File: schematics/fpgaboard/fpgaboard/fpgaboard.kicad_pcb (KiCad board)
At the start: 4 copper layers, 67.6 x 31.1 mm, 2 parts, among them U1 LFE5UM-85F-7BG381x

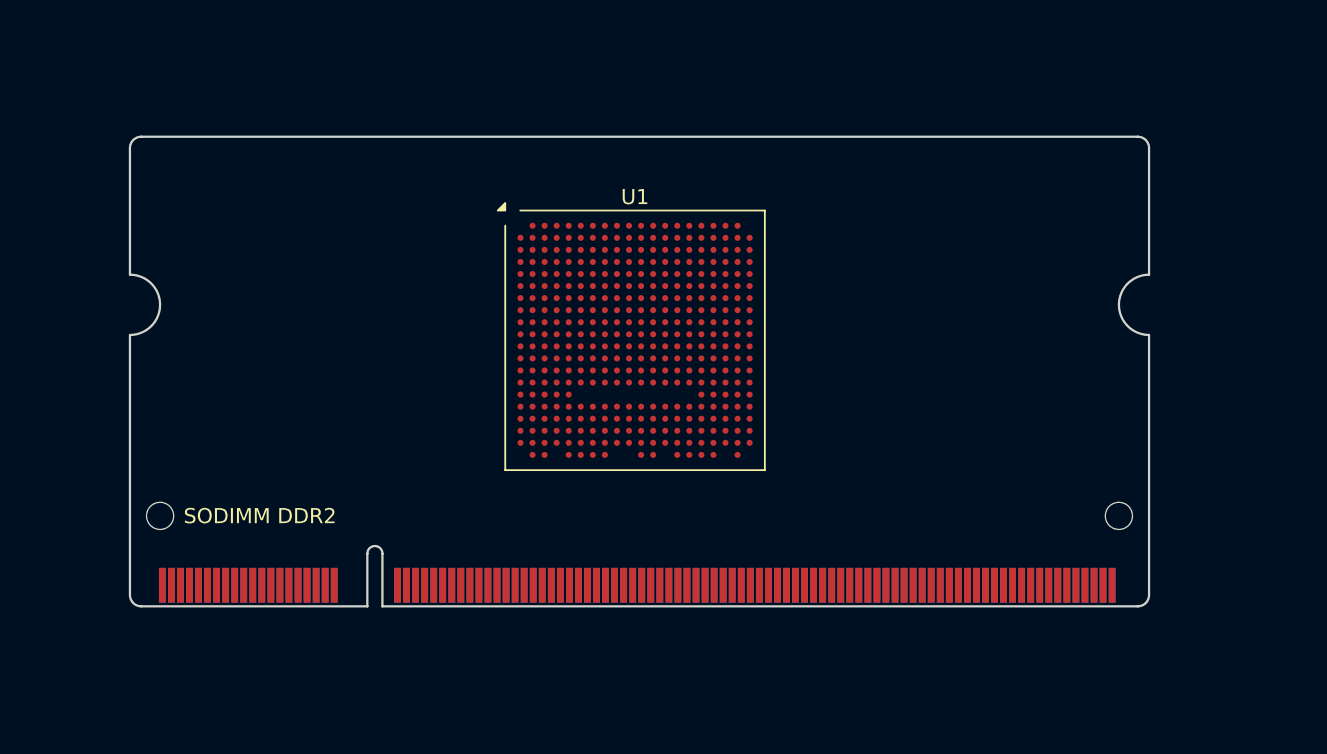
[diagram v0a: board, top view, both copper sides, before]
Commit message: Updated design rules for fpgaboard.
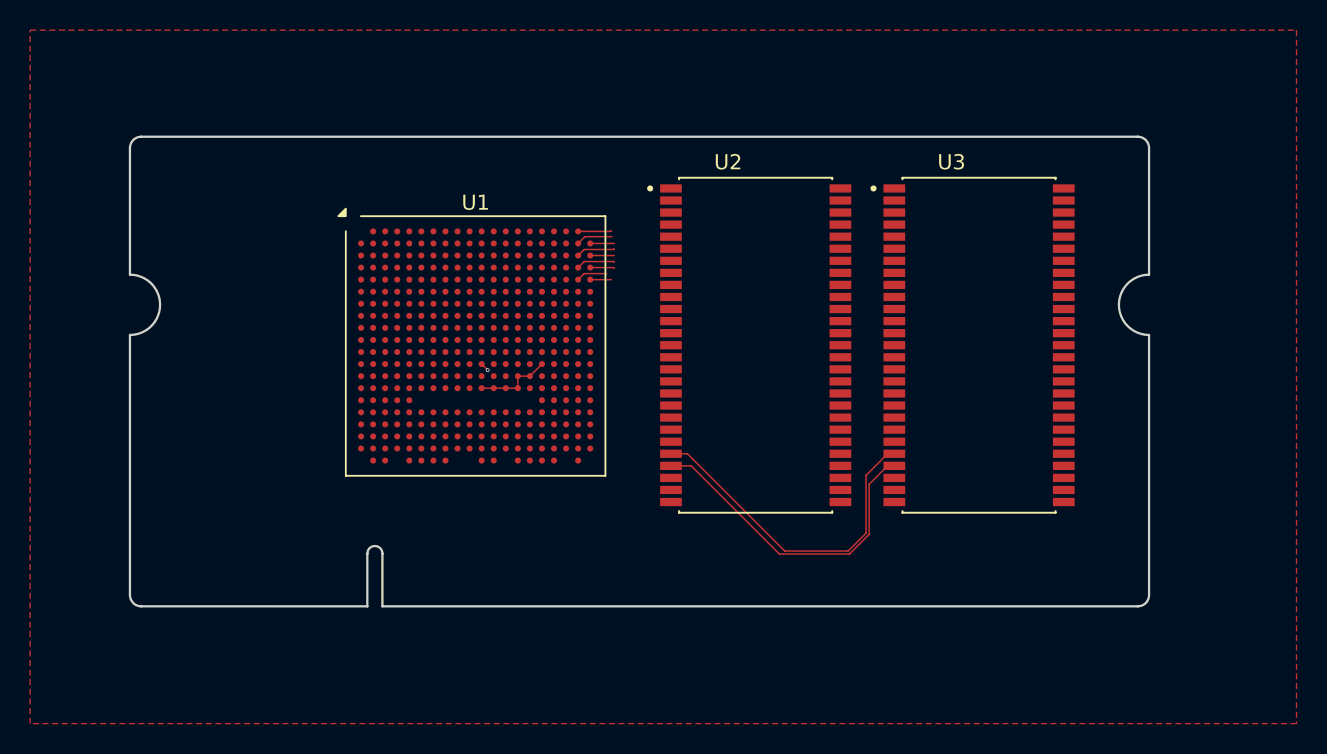
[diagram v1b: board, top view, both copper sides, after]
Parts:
- removed SODIMM DDR2: SODIMM DDR2 EDGE, SODIMM:SODIMM_DDR2_EDGE
- added U2: IS42S16320F-7TL, IS42S16320F-7TL:SOP80P1176X120-54N, F.Cu at (162.1, 79.9)
- added U3: IS42S16320F-7TL, IS42S16320F-7TL:SOP80P1176X120-54N, F.Cu at (176.9, 79.9)
- moved U1 10.6 mm to (143.6, 80.0)
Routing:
- net SDRAM_A0: track 0.00 -> 22.4 mm
- net SDRAM_A1: track 0.00 -> 21.6 mm
- net Net-(U1A-GND-PadB14): track 0.00 -> 8.28 mm, vias 0 -> 1
- net unconnected-(U1D-PR35B-PadD19): track 0.00 -> 2.59 mm
- net unconnected-(U1C-PT119B-PadB19): track 0.00 -> 2.44 mm
- net unconnected-(U1C-PT121A-PadA19): track 0.00 -> 2.22 mm
- net unconnected-(U1D-PR35D-PadE19): track 0.00 -> 2.07 mm
- net unconnected-(U1D-PR35C-PadD20): track 0.00 -> 1.62 mm
- net unconnected-(U1D-PR35A-PadC20): track 0.00 -> 1.60 mm
- net unconnected-(U1C-PT121B-PadB20): track 0.00 -> 1.60 mm
- net unconnected-(U1D-PR38A-PadE20): track 0.00 -> 1.40 mm
- added copper zone on F.Cu, net (none)

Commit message: Work on custom FPGA board with more RAM and beefier FPGA.
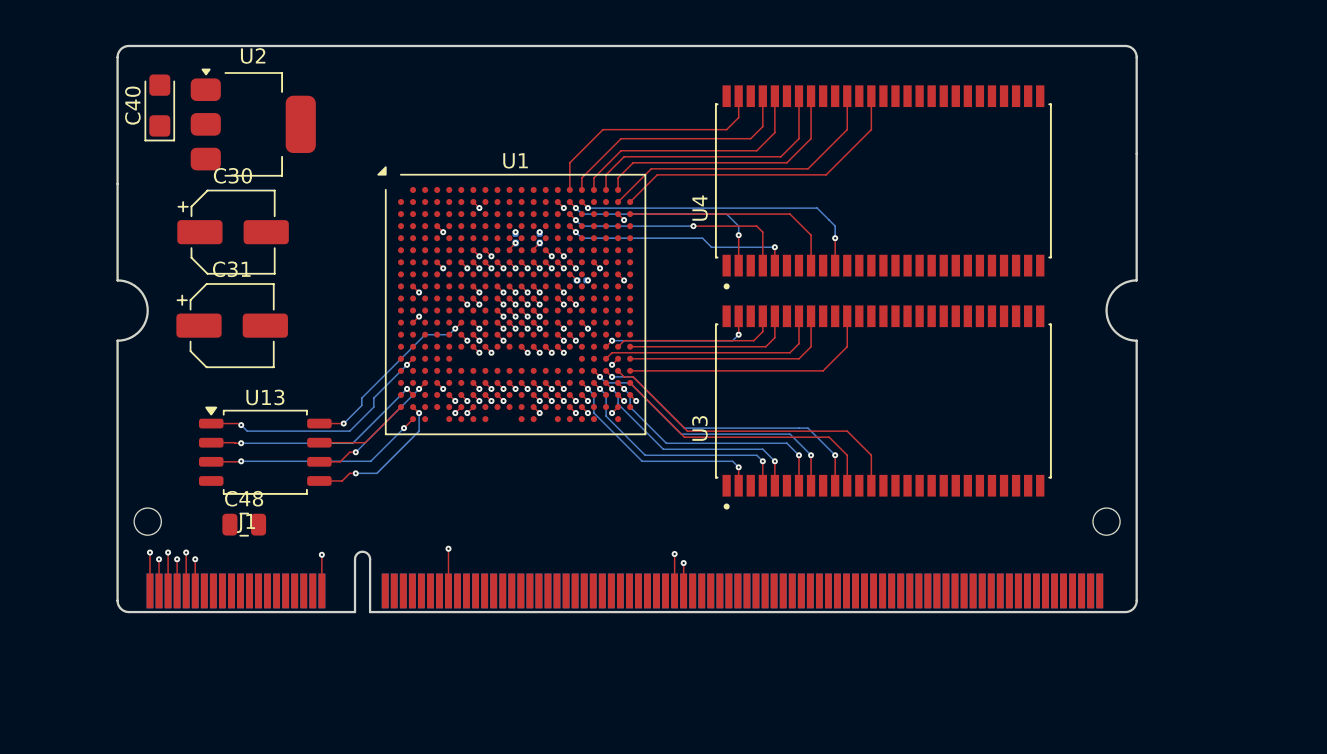
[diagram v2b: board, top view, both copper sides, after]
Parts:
- added C1: C_Small, Capacitor_SMD:C_0201_0603Metric, B.Cu at (146.2, 72.8)
- added C2: C_Small, Capacitor_SMD:C_0201_0603Metric, B.Cu at (147.8, 72.8)
- added C3: C_Small, Capacitor_SMD:C_0201_0603Metric, B.Cu at (150.6, 75.6)
- added C30: 10uF, Capacitor_SMD:CP_Elec_5x5.3, F.Cu at (127.5, 72.4)
- added C31: 22uF, Capacitor_SMD:CP_Elec_5x5.3, F.Cu at (127.4, 78.6)
- added C40: 47uF, Capacitor_Tantalum_SMD:CP_EIA-3216-18_Kemet-A, F.Cu at (122.6, 64.0)
- added C48: 1uF, Capacitor_SMD:C_0805_2012Metric, F.Cu at (128.2, 91.8)
- added J1: SODIMM-200, SODIMM_DDR2_EDGE:SODIMM_DDR2_EDGE, F.Cu at (119.8, 97.6)
- added U13: W25Q32JVSS, Package_SO:SOIC-8_5.3x5.3mm_P1.27mm, F.Cu at (129.6, 87.0)
- added U4: IS42S16320F-7TL, IS42S16320F-7TL:SOP80P1176X120-54N, F.Cu at (170.6, 69.0)
- U1: value LFE5UM-85F-7BG381x -> LFE5UM-85F-8BG381I
- U2: value IS42S16320F-7TL -> AMS1117-3.3; footprint IS42S16320F-7TL:SOP80P1176X120-54N -> Package_TO_SOT_SMD:SOT-223-3_TabPin2
- moved U2 36.4 mm to (128.8, 65.2)
- moved U3 7.34 mm to (170.6, 83.6), turned to 90 degrees
- moved U1 3.82 mm to (146.2, 77.2)
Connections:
- net Net-(U1A-VCC-PadH10) renamed 1v1
- U1 pad A15: unconnected-(U1C-PT103A-PadA15) -> RAM_D31
- U1 pad A16: unconnected-(U1C-PT110A-PadA16) -> RAM_D30
- U1 pad A17: unconnected-(U1C-PT116A-PadA17) -> RAM_D29
- U1 pad A18: unconnected-(U1C-PT119A-PadA18) -> RAM_D28
- U1 pad A19: unconnected-(U1C-PT121A-PadA19) -> RAM_D27
- U1 pad B14: Net-(U1A-GND-PadB14) -> GND
- U1 pad B15: unconnected-(U1C-PT105A-PadB15) -> RAM_D16
- U1 pad B16: unconnected-(U1C-PT110B-PadB16) -> RAM_D21
- U1 pad B19: unconnected-(U1C-PT119B-PadB19) -> RAM_D25
- U1 pad B20: unconnected-(U1C-PT121B-PadB20) -> RAM_D24
- U1 pad B7: Net-(U1A-GND-PadB14) -> GND
- U1 pad C15: unconnected-(U1C-PT105B-PadC15) -> RAM_D17
- U1 pad C16: unconnected-(U1C-PT112A-PadC16) -> RAM_D22
- U1 pad C17: unconnected-(U1C-PT114B-PadC17) -> RAM_D26
- U1 pad C19: Net-(U1A-GND-PadB14) -> GND
- U1 pad C20: unconnected-(U1D-PR35A-PadC20) -> RAM_D20
- U1 pad D15: unconnected-(U1C-PT107A-PadD15) -> RAM_D18
- U1 pad D16: unconnected-(U1C-PT112B-PadD16) -> RAM_D23
- U1 pad D4: Net-(U1A-GND-PadB14) -> GND
- U1 pad E15: unconnected-(U1C-PT107B-PadE15) -> RAM_D19
- U1 pad E19: unconnected-(U1D-PR35D-PadE19) -> RAM_A0
- U1 pad E20: unconnected-(U1D-PR38A-PadE20) -> RAM_A1
- U1 pad F10: Net-(U1B-VCCIO0-PadF10) -> IO_3v3
- U1 pad F11: Net-(U1C-VCCIO1-PadF11) -> IO_3v3
- U1 pad F12: Net-(U1C-VCCIO1-PadF11) -> IO_3v3
- U1 pad F13: Net-(U1A-GND-PadB14) -> GND
- U1 pad F14: Net-(U1A-GND-PadB14) -> GND
- U1 pad F19: unconnected-(U1D-PR38B-PadF19) -> RAM_A2
- U1 pad F20: unconnected-(U1D-PR38C-PadF20) -> RAM_A3
- U1 pad F7: Net-(U1A-GND-PadB14) -> GND
- U1 pad F8: Net-(U1A-GND-PadB14) -> GND
- U1 pad F9: Net-(U1B-VCCIO0-PadF10) -> IO_3v3
- U1 pad G10: Net-(U1A-GND-PadB14) -> GND
- U1 pad G11: Net-(U1A-GND-PadB14) -> GND
- U1 pad G12: Net-(U1A-GND-PadB14) -> GND
- U1 pad G13: Net-(U1A-GND-PadB14) -> GND
- U1 pad G14: Net-(U1A-GND-PadB14) -> GND
- U1 pad G15: Net-(U1A-GND-PadB14) -> GND
- U1 pad G17: Net-(U1A-GND-PadB14) -> GND
- U1 pad G19: unconnected-(U1D-PR41A-PadG19) -> RAM_A5
- U1 pad G20: unconnected-(U1D-PR38D-PadG20) -> RAM_A4
- U1 pad G4: Net-(U1A-GND-PadB14) -> GND
- U1 pad G6: Net-(U1A-GND-PadB14) -> GND
- U1 pad G7: Net-(U1A-GND-PadB14) -> GND
- U1 pad G8: Net-(U1A-GND-PadB14) -> GND
- U1 pad G9: Net-(U1A-GND-PadB14) -> GND
- U1 pad H14: Net-(U1D-VCCIO2-PadH14) -> IO_3v3
- U1 pad H15: Net-(U1D-VCCIO2-PadH14) -> IO_3v3
- U1 pad H19: Net-(U1A-GND-PadB14) -> GND
- U1 pad H20: unconnected-(U1D-PR41B-PadH20) -> RAM_A6
- U1 pad H6: Net-(U1G-VCCIO7-PadH6) -> IO_3v3
- U1 pad H7: Net-(U1G-VCCIO7-PadH6) -> IO_3v3
- U1 pad J10: Net-(U1A-GND-PadB14) -> GND
- U1 pad J11: Net-(U1A-GND-PadB14) -> GND
- U1 pad J12: Net-(U1A-GND-PadB14) -> GND
- U1 pad J14: Net-(U1A-GND-PadB14) -> GND
- U1 pad J15: Net-(U1D-VCCIO2-PadH14) -> IO_3v3
- U1 pad J18: unconnected-(U1D-PR41C-PadJ18) -> RAM_A7
- U1 pad J19: unconnected-(U1D-PR44A-PadJ19) -> RAM_A9
- U1 pad J2: Net-(U1A-GND-PadB14) -> GND
- U1 pad J20: unconnected-(U1D-PR44C-PadJ20) -> RAM_A11
- U1 pad J6: Net-(U1G-VCCIO7-PadH6) -> IO_3v3
- U1 pad J7: Net-(U1A-GND-PadB14) -> GND
- U1 pad J9: Net-(U1A-GND-PadB14) -> GND
- U1 pad K10: Net-(U1A-GND-PadB14) -> GND
- U1 pad K11: Net-(U1A-GND-PadB14) -> GND
- U1 pad K12: Net-(U1A-GND-PadB14) -> GND
- U1 pad K14: Net-(U1A-GND-PadB14) -> GND
- U1 pad K15: Net-(U1A-GND-PadB14) -> GND
- U1 pad K18: unconnected-(U1D-PR41D-PadK18) -> RAM_A8
- U1 pad K19: unconnected-(U1D-PR44B-PadK19) -> RAM_A10
- U1 pad K20: unconnected-(U1D-PR44D-PadK20) -> RAM_A12
- U1 pad K6: Net-(U1A-GND-PadB14) -> GND
- U1 pad K7: Net-(U1A-GND-PadB14) -> GND
- U1 pad K9: Net-(U1A-GND-PadB14) -> GND
- U1 pad L10: Net-(U1A-GND-PadB14) -> GND
- U1 pad L11: Net-(U1A-GND-PadB14) -> GND
- U1 pad L12: Net-(U1A-GND-PadB14) -> GND
- U1 pad L14: Net-(U1E-VCCIO3-PadL14) -> IO_3v3
- U1 pad L15: Net-(U1E-VCCIO3-PadL14) -> IO_3v3
- U1 pad L16: unconnected-(U1E-PR50A-PadL16) -> ~{RAM_CAS}
- U1 pad L17: unconnected-(U1E-PR50B-PadL17) -> ~{RAM_WE}
- U1 pad L19: unconnected-(U1E-PR47C-PadL19) -> ~{RAM_CS}
- U1 pad L20: unconnected-(U1E-PR47A-PadL20) -> RAM_CLK
- U1 pad L6: Net-(U1F-VCCIO6-PadL6) -> IO_3v3
- U1 pad L7: Net-(U1F-VCCIO6-PadL6) -> IO_3v3
- U1 pad L9: Net-(U1A-GND-PadB14) -> GND
- U1 pad M10: Net-(U1A-GND-PadB14) -> GND
- U1 pad M11: Net-(U1A-GND-PadB14) -> GND
- U1 pad M12: Net-(U1A-GND-PadB14) -> GND
- U1 pad M14: Net-(U1A-GND-PadB14) -> GND
- U1 pad M15: Net-(U1E-VCCIO3-PadL14) -> IO_3v3
- U1 pad M16: Net-(U1A-GND-PadB14) -> GND
- U1 pad M19: unconnected-(U1E-PR47D-PadM19) -> ~{RAM_RAS}
- U1 pad M2: Net-(U1A-GND-PadB14) -> GND
- U1 pad M20: unconnected-(U1E-PR47B-PadM20) -> RAM_CKE
- U1 pad M6: Net-(U1F-VCCIO6-PadL6) -> IO_3v3
- U1 pad M7: Net-(U1A-GND-PadB14) -> GND
- U1 pad M9: Net-(U1A-GND-PadB14) -> GND
- U1 pad N14: Net-(U1A-GND-PadB14) -> GND
- U1 pad N15: Net-(U1A-GND-PadB14) -> GND
- U1 pad N19: unconnected-(U1E-PR83A-PadN19) -> RAM_D10
- U1 pad N20: unconnected-(U1E-PR83B-PadN20) -> RAM_D8
- U1 pad N6: Net-(U1A-GND-PadB14) -> GND
- U1 pad N7: Net-(U1A-GND-PadB14) -> GND
- U1 pad P10: Net-(U1H-VCCIO8-PadP10) -> IO_3v3
- U1 pad P11: Net-(U1A-GND-PadB14) -> GND
- U1 pad P12: Net-(U1A-GND-PadB14) -> GND
- U1 pad P13: Net-(U1A-GND-PadB14) -> GND
- U1 pad P14: Net-(U1A-GND-PadB14) -> GND
- U1 pad P18: unconnected-(U1E-PR83D-PadP18) -> RAM_D15
- U1 pad P19: unconnected-(U1E-PR83C-PadP19) -> RAM_D14
- U1 pad P20: unconnected-(U1E-PR86A-PadP20) -> RAM_D13
- U1 pad P7: Net-(U1A-GND-PadB14) -> GND
- U1 pad P8: Net-(U1A-GND-PadB14) -> GND
- U1 pad P9: Net-(U1H-VCCIO8-PadP10) -> IO_3v3
- U1 pad R18: unconnected-(U1E-PR89B-PadR18) -> RAM_D12
- U1 pad R19: Net-(U1A-GND-PadB14) -> GND
- U1 pad R2: unconnected-(U1H-PB15A-PadR2) -> FLASH_CSn
- U1 pad R20: unconnected-(U1E-PR86B-PadR20) -> RAM_D11
- U1 pad R4: unconnected-(U1I-CFG_2-PadR4) -> GND
- U1 pad R5: unconnected-(U1I-TDI-PadR5) -> JTAG_TDI
- U1 pad T17: unconnected-(U1E-PR92D-PadT17) -> RAM_D4
- U1 pad T18: unconnected-(U1E-PR89D-PadT18) -> RAM_D5
- U1 pad T19: unconnected-(U1E-PR89A-PadT19) -> RAM_D7
- U1 pad T20: unconnected-(U1E-PR86C-PadT20) -> RAM_D9
- U1 pad T4: unconnected-(U1I-CFG_1-PadT4) -> Net-(U1I-CFG_1)
- U1 pad T5: unconnected-(U1I-TCK-PadT5) -> JTAG_TCK
- U1 pad U10: Net-(U1A-GND-PadB14) -> GND
- U1 pad U11: Net-(U1A-GND-PadB14) -> GND
- U1 pad U12: Net-(U1A-GND-PadB14) -> GND
- U1 pad U13: Net-(U1A-GND-PadB14) -> GND
- U1 pad U14: Net-(U1A-GND-PadB14) -> GND
- U1 pad U16: unconnected-(U1E-PR92C-PadU16) -> RAM_D0
- U1 pad U17: unconnected-(U1E-PR92B-PadU17) -> RAM_D1
- U1 pad U18: unconnected-(U1E-PR92A-PadU18) -> RAM_D2
- U1 pad U19: unconnected-(U1E-PR89C-PadU19) -> RAM_D3
- U1 pad U20: unconnected-(U1E-PR86D-PadU20) -> RAM_D6
- U1 pad U3: unconnected-(U1I-CCLK-PadU3) -> FLASH_CLK
- U1 pad U4: unconnected-(U1I-CFG_0-PadU4) -> GND
- U1 pad U5: unconnected-(U1I-TMS-PadU5) -> JTAG_TMS
- U1 pad U7: Net-(U1A-GND-PadB14) -> GND
- U1 pad U8: Net-(U1A-GND-PadB14) -> GND
- U1 pad U9: Net-(U1A-GND-PadB14) -> GND
- U1 pad V12: Net-(U1A-GND-PadB14) -> GND
- U1 pad V13: Net-(U1A-GND-PadB14) -> GND
- U1 pad V14: Net-(U1A-GND-PadB14) -> GND
- U1 pad V15: Net-(U1A-GND-PadB14) -> GND
- U1 pad V16: Net-(U1A-GND-PadB14) -> GND
- U1 pad V19: Net-(U1A-GND-PadB14) -> GND
- U1 pad V2: unconnected-(U1H-PB11A-PadV2) -> FLASH_IO1
- U1 pad V20: Net-(U1A-GND-PadB14) -> GND
- U1 pad V3: unconnected-(U1I-~{INIT}-PadV3) -> Net-(U1I-~{INIT})
- U1 pad V4: unconnected-(U1I-TDO-PadV4) -> JTAG_TDO
- U1 pad V5: Net-(U1A-GND-PadB14) -> GND
- U1 pad V6: Net-(U1A-GND-PadB14) -> GND
- U1 pad V7: Net-(U1A-GND-PadB14) -> GND
- U1 pad V8: Net-(U1A-GND-PadB14) -> GND
- U1 pad V9: Net-(U1A-GND-PadB14) -> GND
- U1 pad W1: unconnected-(U1H-PB9A-PadW1) -> FLASH_IO3
- U1 pad W12: Net-(U1A-GND-PadB14) -> GND
- U1 pad W15: Net-(U1A-GND-PadB14) -> GND
- U1 pad W16: Net-(U1A-GND-PadB14) -> GND
- U1 pad W19: Net-(U1A-GND-PadB14) -> GND
- U1 pad W2: unconnected-(U1H-PB11B-PadW2) -> FLASH_IO0
- U1 pad W3: unconnected-(U1I-~{PROGRAM}-PadW3) -> Net-(U1I-~{PROGRAM})
- U1 pad W6: Net-(U1A-GND-PadB14) -> GND
- U1 pad W7: Net-(U1A-GND-PadB14) -> GND
- U1 pad Y2: unconnected-(U1H-PB9B-PadY2) -> FLASH_IO2
- U2 pad 1: Net-(U2-VDD-Pad1) -> GND
- U2 pad 2: unconnected-(U2-DQ0-Pad2) -> IO_3v3
- U2 pad 3: Net-(U2-VDDQ-Pad3) -> 5V0
- U3 pad 10: unconnected-(U3-DQ5-Pad10) -> RAM_D5
- U3 pad 11: unconnected-(U3-DQ6-Pad11) -> RAM_D6
- U3 pad 13: unconnected-(U3-DQ7-Pad13) -> RAM_D7
- U3 pad 16: unconnected-(U3-~{WE}-Pad16) -> ~{RAM_WE}
- U3 pad 17: unconnected-(U3-~{CAS}-Pad17) -> ~{RAM_CAS}
- U3 pad 18: unconnected-(U3-~{RAS}-Pad18) -> ~{RAM_RAS}
- U3 pad 19: unconnected-(U3-~{CS}-Pad19) -> ~{RAM_CS}
- U3 pad 2: unconnected-(U3-DQ0-Pad2) -> RAM_D0
- U3 pad 20: unconnected-(U3-BA0-Pad20) -> RAM_BA0
- U3 pad 21: unconnected-(U3-BA1-Pad21) -> RAM_BA1
- U3 pad 22: unconnected-(U3-A10-Pad22) -> RAM_A10
- U3 pad 23: SDRAM_A0 -> RAM_A0
- U3 pad 24: SDRAM_A1 -> RAM_A1
- U3 pad 25: unconnected-(U3-A2-Pad25) -> RAM_A2
- U3 pad 26: unconnected-(U3-A3-Pad26) -> RAM_A3
- U3 pad 29: unconnected-(U3-A4-Pad29) -> RAM_A4
- U3 pad 30: unconnected-(U3-A5-Pad30) -> RAM_A5
- U3 pad 31: unconnected-(U3-A6-Pad31) -> RAM_A6
- U3 pad 32: unconnected-(U3-A7-Pad32) -> RAM_A7
- U3 pad 33: unconnected-(U3-A8-Pad33) -> RAM_A8
- U3 pad 34: unconnected-(U3-A9-Pad34) -> RAM_A9
- U3 pad 35: unconnected-(U3-A11-Pad35) -> RAM_A11
- U3 pad 36: unconnected-(U3-A12-Pad36) -> RAM_A12
- U3 pad 37: unconnected-(U3-CKE-Pad37) -> RAM_CKE
- U3 pad 38: unconnected-(U3-CLK-Pad38) -> RAM_CLK
- U3 pad 4: unconnected-(U3-DQ1-Pad4) -> RAM_D1
- U3 pad 42: unconnected-(U3-DQ8-Pad42) -> RAM_D8
- U3 pad 44: unconnected-(U3-DQ9-Pad44) -> RAM_D9
- U3 pad 45: unconnected-(U3-DQ10-Pad45) -> RAM_D10
- U3 pad 47: unconnected-(U3-DQ11-Pad47) -> RAM_D11
- U3 pad 48: unconnected-(U3-DQ12-Pad48) -> RAM_D12
- U3 pad 5: unconnected-(U3-DQ2-Pad5) -> RAM_D2
- U3 pad 50: unconnected-(U3-DQ13-Pad50) -> RAM_D13
- U3 pad 51: unconnected-(U3-DQ14-Pad51) -> RAM_D14
- U3 pad 53: unconnected-(U3-DQ15-Pad53) -> RAM_D15
- U3 pad 7: unconnected-(U3-DQ3-Pad7) -> RAM_D3
- U3 pad 8: unconnected-(U3-DQ4-Pad8) -> RAM_D4
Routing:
- net GND: track 0.00 -> 72.3 mm, vias 0 -> 99
- net SDRAM_A0: track 22.4 -> 0.00 mm
- net SDRAM_A1: track 21.6 -> 0.00 mm
- net RAM_D7: track 0.00 -> 21.1 mm
- net RAM_D24: track 0.00 -> 20.2 mm
- net RAM_D21: track 0.00 -> 20.1 mm, vias 0 -> 2
- net RAM_D5: track 0.00 -> 19.5 mm, vias 0 -> 2
- net RAM_D25: track 0.00 -> 19.4 mm
- net RAM_D4: track 0.00 -> 18.7 mm, vias 0 -> 2
- net RAM_D6: track 0.00 -> 18.4 mm
- net RAM_D28: track 0.00 -> 17.6 mm
- net RAM_D27: track 0.00 -> 17.5 mm
- net RAM_D9: track 0.00 -> 17.1 mm
- net RAM_D3: track 0.00 -> 16.5 mm, vias 0 -> 2
- net RAM_D29: track 0.00 -> 16.5 mm
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- added copper zone on In2.Cu, net 1v1
- added copper zone on In1.Cu, net GND
- removed copper zone on F.Cu, net (none)
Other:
- board size 67.6 x 31.1 mm -> 67.6 x 37.5 mm

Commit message: Some work on FPGA board, adding some decoupling, SODIMM signals etc.
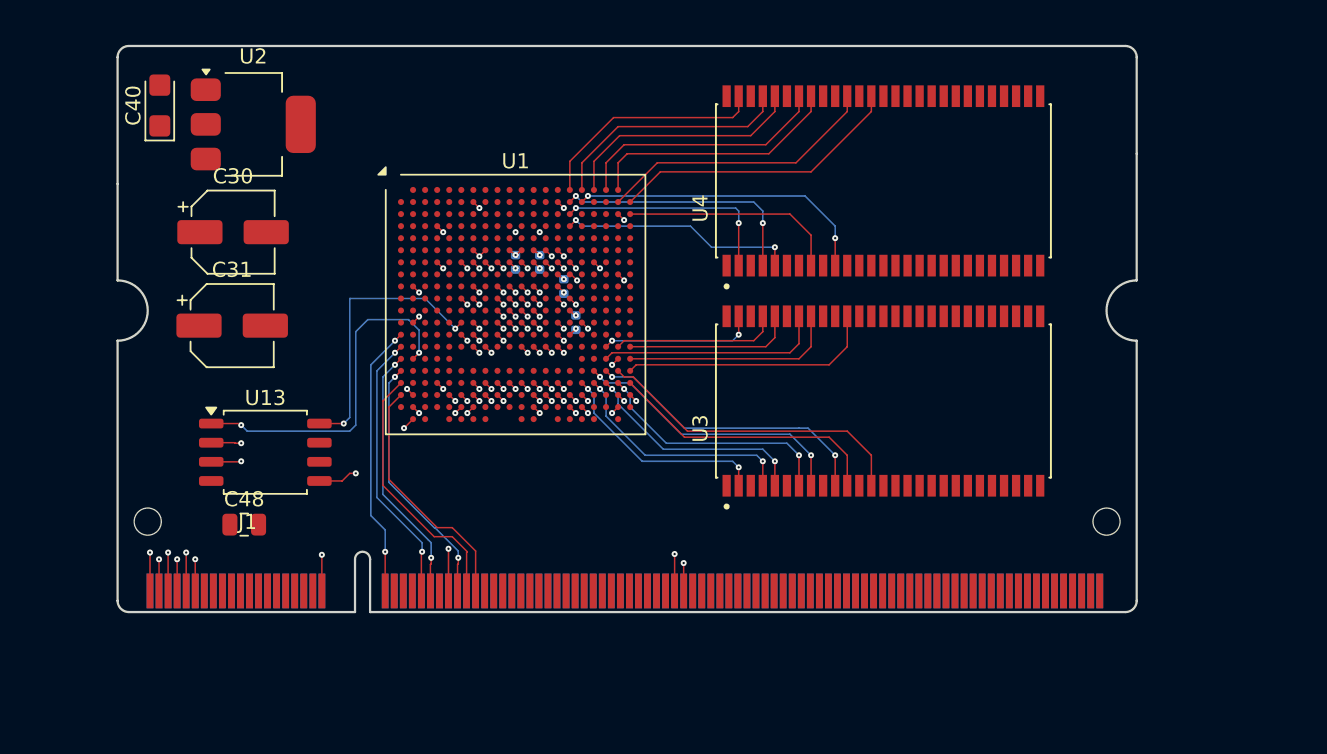
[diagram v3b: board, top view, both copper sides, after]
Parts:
- added C4: C_Small, Capacitor_SMD:C_0402_1005Metric, B.Cu at (150.2, 78.4)
- C1, C2, C3: footprint Capacitor_SMD:C_0201_0603Metric -> Capacitor_SMD:C_0402_1005Metric
- moved C1 1.60 mm to (146.2, 74.4), turned to -90 degrees
- moved C2 1.60 mm to (147.8, 74.4), turned to -90 degrees
- moved C3 1.26 mm to (149.4, 76.0), turned to -90 degrees
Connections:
- J1 pad 100: unconnected-(J1-Pad100) -> S80
- J1 pad 101: unconnected-(J1-Pad101) -> S26
- J1 pad 102: unconnected-(J1-Pad102) -> S81
- J1 pad 103: unconnected-(J1-Pad103) -> S27
- J1 pad 104: unconnected-(J1-Pad104) -> S82
- J1 pad 109: unconnected-(J1-Pad109) -> S28
- J1 pad 110: unconnected-(J1-Pad110) -> S83
- J1 pad 111: unconnected-(J1-Pad111) -> S29
- J1 pad 112: unconnected-(J1-Pad112) -> S84
- J1 pad 113: unconnected-(J1-Pad113) -> S30
- J1 pad 114: unconnected-(J1-Pad114) -> S85
- J1 pad 115: unconnected-(J1-Pad115) -> S31
- J1 pad 116: unconnected-(J1-Pad116) -> S86
- J1 pad 117: unconnected-(J1-Pad117) -> S32
- J1 pad 118: unconnected-(J1-Pad118) -> S87
- J1 pad 119: unconnected-(J1-Pad119) -> S33
- J1 pad 120: unconnected-(J1-Pad120) -> S88
- J1 pad 121: unconnected-(J1-Pad121) -> S34
- J1 pad 122: unconnected-(J1-Pad122) -> S89
- J1 pad 123: unconnected-(J1-Pad123) -> S35
- J1 pad 124: unconnected-(J1-Pad124) -> S90
- J1 pad 125: unconnected-(J1-Pad125) -> S36
- J1 pad 126: unconnected-(J1-Pad126) -> S91
- J1 pad 127: unconnected-(J1-Pad127) -> S37
- J1 pad 128: unconnected-(J1-Pad128) -> S92
- J1 pad 129: unconnected-(J1-Pad129) -> S38
- J1 pad 130: unconnected-(J1-Pad130) -> S93
- J1 pad 131: unconnected-(J1-Pad131) -> S39
- J1 pad 132: unconnected-(J1-Pad132) -> S94
- J1 pad 133: unconnected-(J1-Pad133) -> S40
- J1 pad 134: unconnected-(J1-Pad134) -> S95
- J1 pad 135: unconnected-(J1-Pad135) -> S41
- J1 pad 136: unconnected-(J1-Pad136) -> S96
- J1 pad 137: unconnected-(J1-Pad137) -> S42
- J1 pad 138: unconnected-(J1-Pad138) -> S97
- J1 pad 139: unconnected-(J1-Pad139) -> S43
- J1 pad 140: unconnected-(J1-Pad140) -> S98
- J1 pad 141: unconnected-(J1-Pad141) -> S44
- J1 pad 142: unconnected-(J1-Pad142) -> S99
- J1 pad 143: unconnected-(J1-Pad143) -> S45
- J1 pad 144: unconnected-(J1-Pad144) -> S100
- J1 pad 145: unconnected-(J1-Pad145) -> S46
- J1 pad 146: unconnected-(J1-Pad146) -> S101
- J1 pad 147: unconnected-(J1-Pad147) -> S47
- J1 pad 148: unconnected-(J1-Pad148) -> S102
- J1 pad 149: unconnected-(J1-Pad149) -> S48
- J1 pad 150: unconnected-(J1-Pad150) -> S103
- J1 pad 151: unconnected-(J1-Pad151) -> S49
- J1 pad 152: unconnected-(J1-Pad152) -> S104
- J1 pad 153: unconnected-(J1-Pad153) -> S50
- J1 pad 154: unconnected-(J1-Pad154) -> S105
- J1 pad 155: unconnected-(J1-Pad155) -> S51
- J1 pad 156: unconnected-(J1-Pad156) -> S106
- J1 pad 41: PT29B -> S1
- J1 pad 42: unconnected-(J1-Pad42) -> S52
- J1 pad 44: unconnected-(J1-Pad44) -> S53
- J1 pad 46: unconnected-(J1-Pad46) -> S54
- J1 pad 48: unconnected-(J1-Pad48) -> S55
- J1 pad 49: unconnected-(J1-Pad49) -> S2
- J1 pad 50: unconnected-(J1-Pad50) -> S56
- J1 pad 51: unconnected-(J1-Pad51) -> S3
- J1 pad 52: unconnected-(J1-Pad52) -> S57
- J1 pad 54: unconnected-(J1-Pad54) -> S58
- J1 pad 57: unconnected-(J1-Pad57) -> S4
- J1 pad 58: unconnected-(J1-Pad58) -> S59
- J1 pad 59: unconnected-(J1-Pad59) -> S5
- J1 pad 60: unconnected-(J1-Pad60) -> S60
- J1 pad 61: unconnected-(J1-Pad61) -> S6
- J1 pad 62: unconnected-(J1-Pad62) -> S61
- J1 pad 63: unconnected-(J1-Pad63) -> S7
- J1 pad 64: unconnected-(J1-Pad64) -> S62
- J1 pad 65: unconnected-(J1-Pad65) -> S8
- J1 pad 66: unconnected-(J1-Pad66) -> S63
- J1 pad 67: unconnected-(J1-Pad67) -> S9
- J1 pad 68: unconnected-(J1-Pad68) -> S64
- J1 pad 69: unconnected-(J1-Pad69) -> S10
- J1 pad 70: unconnected-(J1-Pad70) -> S65
- J1 pad 71: unconnected-(J1-Pad71) -> S11
- J1 pad 72: unconnected-(J1-Pad72) -> S66
- J1 pad 73: unconnected-(J1-Pad73) -> S12
- J1 pad 74: unconnected-(J1-Pad74) -> S67
- J1 pad 75: unconnected-(J1-Pad75) -> S13
- J1 pad 76: unconnected-(J1-Pad76) -> S68
- J1 pad 77: unconnected-(J1-Pad77) -> S14
- J1 pad 78: unconnected-(J1-Pad78) -> S69
- J1 pad 79: unconnected-(J1-Pad79) -> S15
- J1 pad 80: unconnected-(J1-Pad80) -> S70
- J1 pad 81: unconnected-(J1-Pad81) -> S16
- J1 pad 82: unconnected-(J1-Pad82) -> S71
- J1 pad 83: unconnected-(J1-Pad83) -> S17
- J1 pad 84: unconnected-(J1-Pad84) -> S72
- J1 pad 85: unconnected-(J1-Pad85) -> S18
- J1 pad 86: unconnected-(J1-Pad86) -> S73
- J1 pad 87: unconnected-(J1-Pad87) -> S19
- J1 pad 88: unconnected-(J1-Pad88) -> S74
- J1 pad 89: unconnected-(J1-Pad89) -> S20
- J1 pad 90: unconnected-(J1-Pad90) -> S75
- J1 pad 91: unconnected-(J1-Pad91) -> S21
- J1 pad 92: unconnected-(J1-Pad92) -> S76
- J1 pad 93: unconnected-(J1-Pad93) -> S22
- J1 pad 94: unconnected-(J1-Pad94) -> S77
- J1 pad 95: unconnected-(J1-Pad95) -> S23
- J1 pad 96: unconnected-(J1-Pad96) -> S78
- J1 pad 97: unconnected-(J1-Pad97) -> S24
- J1 pad 98: unconnected-(J1-Pad98) -> S79
- J1 pad 99: unconnected-(J1-Pad99) -> S25
- U1 pad B15: RAM_D16 -> RAM_D17
- U1 pad C15: RAM_D17 -> RAM_D16
- U1 pad N1: unconnected-(U1F-PL89D-PadN1) -> S1
- U1 pad P1: unconnected-(U1F-PL92A-PadP1) -> S2
- U1 pad R1: unconnected-(U1H-PB4A-PadR1) -> S3
- U1 pad T1: unconnected-(U1H-PB4B-PadT1) -> S4
- U1 pad U1: unconnected-(U1H-PB6A-PadU1) -> S5
- U1 pad V1: unconnected-(U1H-PB6B-PadV1) -> S6
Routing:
- net S1: track 0.00 -> 18.2 mm, vias 0 -> 2
- net S2: track 0.00 -> 18.1 mm, vias 0 -> 2
- net S5: track 0.00 -> 17.3 mm
- net S3: track 0.00 -> 17.2 mm, vias 0 -> 2
- net S4: track 0.00 -> 16.9 mm, vias 0 -> 2
- net S6: track 0.00 -> 16.3 mm
- net FLASH_IO1: track 15.1 -> 2.57 mm
- net FLASH_IO2: track 14.6 -> 2.85 mm
- net FLASH_CLK: track 9.18 -> 0.00 mm, vias 2 -> 0
- net IO_3v3: track 14.5 -> 21.8 mm, vias 5 -> 7
- net FLASH_CSn: track 15.9 -> 23.0 mm
- net FLASH_IO0: track 9.75 -> 3.19 mm
- net FLASH_IO3: track 6.39 -> 0.00 mm
- net RAM_D17: track 15.5 -> 17.0 mm
- net RAM_D24: track 20.2 -> 19.5 mm
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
